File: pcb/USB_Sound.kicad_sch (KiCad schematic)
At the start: 36 parts, among them IC1 PCM2706, J1 USB4500-03-0-A_REVA, J2 Conn_Coaxial_x2, U5 FSUSB42MUX, U6 24AA02-OT, Y1 Crystal

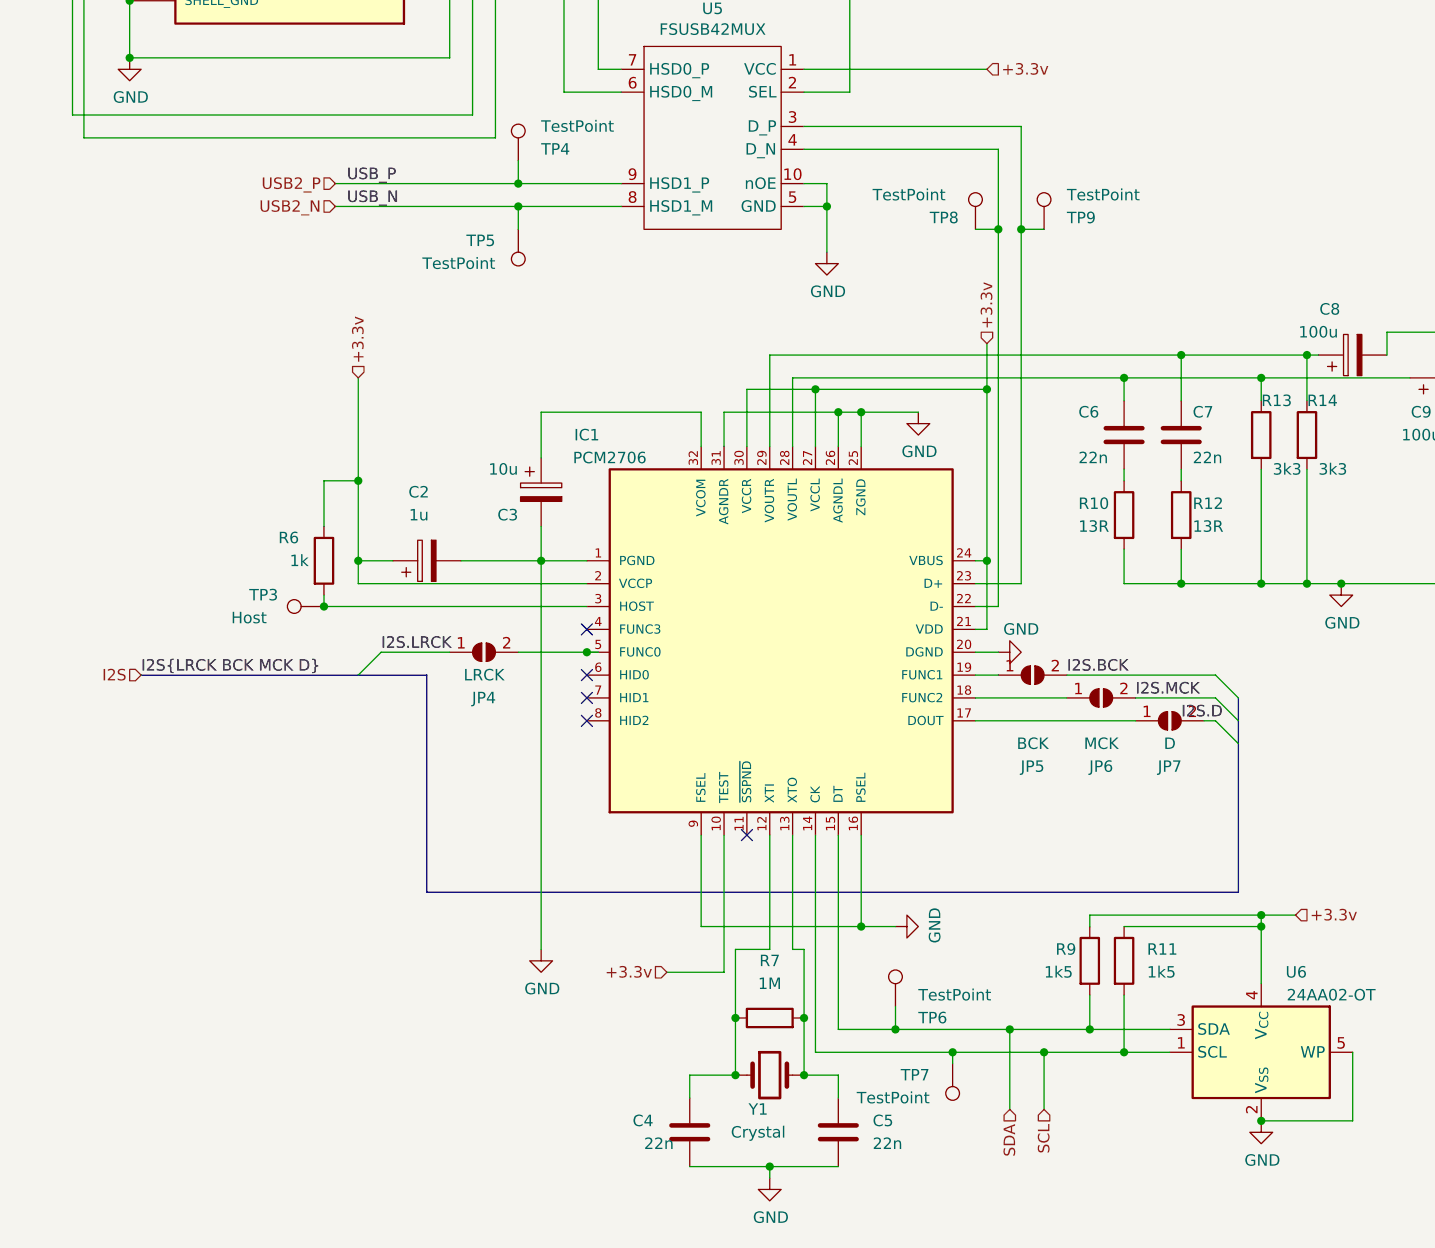
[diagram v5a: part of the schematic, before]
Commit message: - cleanup ERC errors
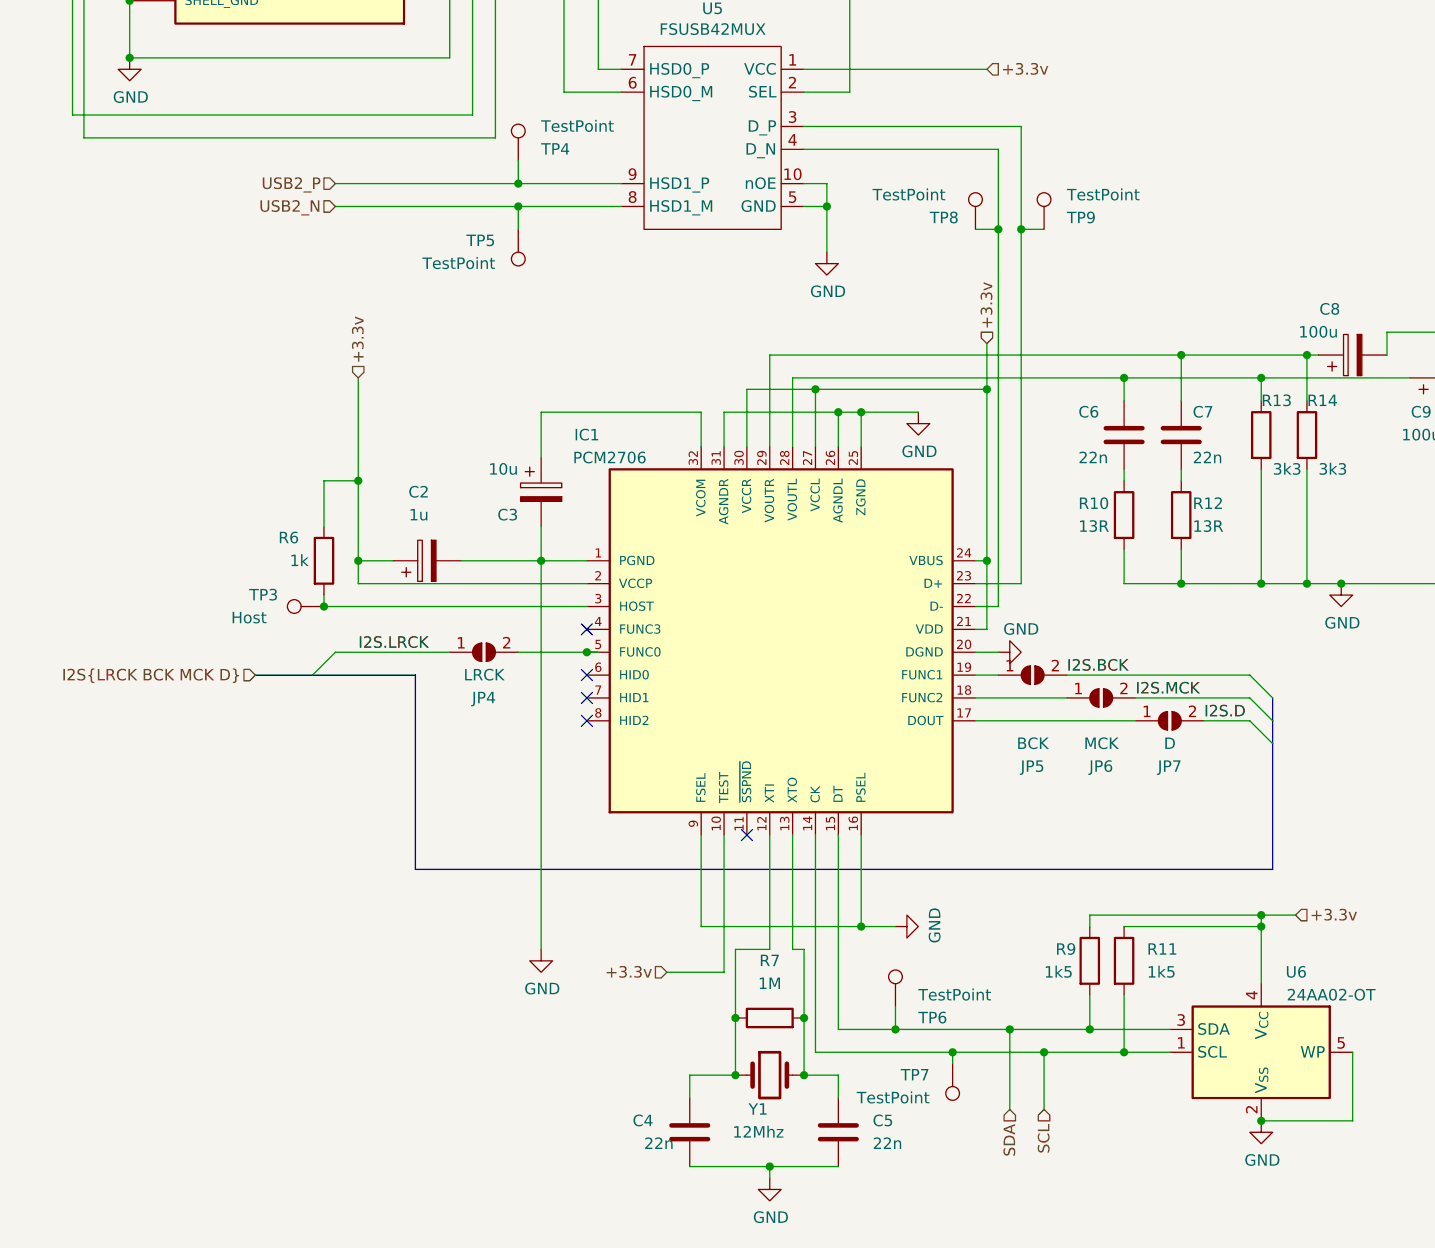
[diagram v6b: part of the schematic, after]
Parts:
- C2, C3, C8, C9: footprint (none) -> Capacitor_SMD:CP_Elec_6.3x7.7
- IC1: footprint Libraries:TQFP32-08 -> Footprints:TQFP32-08
- J1: footprint USB4500-03-0-A_REVA:GCT_USB4500-03-0-A_REVA -> Footprints:GCT_USB4500-03-0-A_REVA
- Y1: value Crystal -> 12Mhz; footprint (none) -> Crystal:Crystal_SMD_Abracon_ABM3-2Pin_5.0x3.2mm_HandSoldering; Farnell (none) -> 2101327
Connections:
- net I2S.D: now also JP7.2 (B)
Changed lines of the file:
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@@
   (no_connect (at 60.96 48.26))
   (no_connect (at 76.2 135.89))
-  (bus_entry (at 148.59 140.97) (size -2.54 -2.54)
-    (stroke (width 0) (type default))
-  )
-  (bus_entry (at 148.59 143.51) (size -2.54 -2.54)
-    (stroke (width 0) (type default))
-  )
-  (bus_entry (at 50.8 135.89) (size 2.54 -2.54)
-    (stroke (width 0) (type default))
-  )
-  (bus_entry (at 148.59 138.43) (size -2.54 -2.54)
+  (bus_entry (at 152.4 143.51) (size -2.54 -2.54)
+    (stroke (width 0) (type default))
+  )
+  (bus_entry (at 45.72 135.89) (size 2.54 -2.54)
+    (stroke (width 0) (type default))
+  )
+  (bus_entry (at 152.4 140.97) (size -2.54 -2.54)
+    (stroke (width 0) (type default))
+  )
+  (bus_entry (at 152.4 138.43) (size -2.54 -2.54)
     (stroke (width 0) (type default))
   )
@@
     (stroke (width 0) (type default))
   )
+  (bus (pts (xy 39.37 135.89) (xy 45.72 135.89))
+    (stroke (width 0) (type default))
+  )
   (wire (pts (xy 96.52 190.5) (xy 96.52 191.77))
     (stroke (width 0) (type default))
@@
     (stroke (width 0) (type default))
   )
-  (wire (pts (xy 53.34 133.35) (xy 60.96 133.35))
-    (stroke (width 0) (type default))
-  )
   (wire (pts (xy 68.58 83.82) (xy 80.01 83.82))
     (stroke (width 0) (type default))
@@
     (stroke (width 0) (type default))
   )
+  (bus (pts (xy 45.72 135.89) (xy 57.15 135.89))
+    (stroke (width 0) (type default))
+  )
   (wire (pts (xy 91.44 106.68) (xy 91.44 110.49))
     (stroke (width 0) (type default))
@@
     (stroke (width 0) (type default))
   )
-  (bus (pts (xy 58.42 160.02) (xy 58.42 135.89))
-    (stroke (width 0) (type default))
-  )
   (wire (pts (xy 119.38 135.89) (xy 121.92 135.89))
     (stroke (width 0) (type default))
@@
     (stroke (width 0) (type default))
   )
+  (wire (pts (xy 137.16 138.43) (xy 149.86 138.43))
+    (stroke (width 0) (type default))
+  )
   (wire (pts (xy 87.63 180.34) (xy 87.63 182.88))
     (stroke (width 0) (type default))
@@
     (stroke (width 0) (type default))
   )
+  (wire (pts (xy 149.86 135.89) (xy 129.54 135.89))
+    (stroke (width 0) (type default))
+  )
   (wire (pts (xy 100.33 83.82) (xy 102.87 83.82))
     (stroke (width 0) (type default))
   )
-  (wire (pts (xy 137.16 138.43) (xy 146.05 138.43))
-    (stroke (width 0) (type default))
-  )
   (wire (pts (xy 25.4 55.88) (xy 25.4 60.96))
     (stroke (width 0) (type default))
@@
     (stroke (width 0) (type default))
   )
-  (bus (pts (xy 50.8 135.89) (xy 58.42 135.89))
-    (stroke (width 0) (type default))
-  )
   (wire (pts (xy 101.6 104.14) (xy 93.98 104.14))
     (stroke (width 0) (type default))
@@
     (stroke (width 0) (type default))
   )
+  (wire (pts (xy 144.78 140.97) (xy 149.86 140.97))
+    (stroke (width 0) (type default))
+  )
   (wire (pts (xy 120.65 104.14) (xy 120.65 123.19))
     (stroke (width 0) (type default))
@@
     (stroke (width 0) (type default))
   )
-  (bus (pts (xy 148.59 160.02) (xy 58.42 160.02))
-    (stroke (width 0) (type default))
-  )
   (wire (pts (xy 62.23 123.19) (xy 71.12 123.19))
     (stroke (width 0) (type default))
   )
-  (wire (pts (xy 146.05 135.89) (xy 129.54 135.89))
-    (stroke (width 0) (type default))
-  )
   (wire (pts (xy 104.14 190.5) (xy 96.52 190.5))
     (stroke (width 0) (type default))
@@
     (stroke (width 0) (type default))
   )
+  (bus (pts (xy 57.15 135.89) (xy 57.15 157.48))
+    (stroke (width 0) (type default))
+  )
   (wire (pts (xy 132.08 171.45) (xy 132.08 175.26))
     (stroke (width 0) (type default))
@@
     (stroke (width 0) (type default))
   )
-  (bus (pts (xy 148.59 143.51) (xy 148.59 160.02))
-    (stroke (width 0) (type default))
-  )
   (wire (pts (xy 101.6 153.67) (xy 101.6 177.8))
     (stroke (width 0) (type default))
@@
     (stroke (width 0) (type default))
   )
-  (bus (pts (xy 26.67 135.89) (xy 50.8 135.89))
-    (stroke (width 0) (type default))
-  )
   (wire (pts (xy 25.4 67.31) (xy 25.4 60.96))
     (stroke (width 0) (type default))
@@
     (stroke (width 0) (type default))
   )
+  (wire (pts (xy 48.26 133.35) (xy 60.96 133.35))
+    (stroke (width 0) (type default))
+  )
   (wire (pts (xy 48.26 81.28) (xy 68.58 81.28))
     (stroke (width 0) (type default))
@@
     (stroke (width 0) (type default))
   )
-  (bus (pts (xy 148.59 138.43) (xy 148.59 140.97))
-    (stroke (width 0) (type default))
-  )
   (wire (pts (xy 76.2 133.35) (xy 77.47 133.35))
     (stroke (width 0) (type default))
@@
     (stroke (width 0) (type default))
   )
+  (bus (pts (xy 152.4 143.51) (xy 152.4 157.48))
+    (stroke (width 0) (type default))
+  )
   (wire (pts (xy 50.8 114.3) (xy 50.8 123.19))
     (stroke (width 0) (type default))
@@
     (stroke (width 0) (type default))
   )
+  (bus (pts (xy 152.4 138.43) (xy 152.4 140.97))
+    (stroke (width 0) (type default))
+  )
   (wire (pts (xy 88.9 153.67) (xy 88.9 163.83))
     (stroke (width 0) (type default))
@@
     (stroke (width 0) (type default))
   )
+  (bus (pts (xy 57.15 157.48) (xy 152.4 157.48))
+    (stroke (width 0) (type default))
+  )
   (wire (pts (xy 76.2 128.27) (xy 46.99 128.27))
     (stroke (width 0) (type default))
@@
     (stroke (width 0) (type default))
   )
-  (bus (pts (xy 148.59 140.97) (xy 148.59 143.51))
-    (stroke (width 0) (type default))
-  )
   (wire (pts (xy 92.71 180.34) (xy 87.63 180.34))
     (stroke (width 0) (type default))
@@
     (stroke (width 0) (type default))
   )
+  (bus (pts (xy 152.4 140.97) (xy 152.4 143.51))
+    (stroke (width 0) (type default))
+  )
   (wire (pts (xy 106.68 163.83) (xy 110.49 163.83))
     (stroke (width 0) (type default))
@@
     (stroke (width 0) (type default))
   )
-  (wire (pts (xy 144.78 140.97) (xy 146.05 140.97))
-    (stroke (width 0) (type default))
-  )
   (wire (pts (xy 135.89 102.87) (xy 151.13 102.87))
     (stroke (width 0) (type default))
@@
   (wire (pts (xy 119.38 130.81) (xy 120.65 130.81))
     (stroke (width 0) (type default))
-  )
-  (label "I2S{LRCK BCK MCK D}" (at 26.67 135.89 0) (fields_autoplaced)
-    (effects (font (size 1.27 1.27)) (justify left bottom))
   )
   (label "I2S.MCK" (at 137.16 138.43 0)
     (effects (font (size 1.27 1.27)) (justify left bottom))
   )
-  (label "USB_P" (at 49.53 81.28 0) (fields_autoplaced)
-    (effects (font (size 1.27 1.27)) (justify left bottom))
-  )
   (label "USBD_P" (at 69.85 43.18 0) (fields_autoplaced)
     (effects (font (size 1.27 1.27)) (justify left bottom))
   )
-  (label "I2S.D" (at 142.24 140.97 0)
-    (effects (font (size 1.27 1.27)) (justify left bottom))
-  )
   (label "USBD_N" (at 69.85 45.72 0) (fields_autoplaced)
     (effects (font (size 1.27 1.27)) (justify left bottom))
   )
-  (label "I2S.LRCK" (at 53.34 133.35 0)
+  (label "I2S.LRCK" (at 50.8 133.35 0)
     (effects (font (size 1.27 1.27)) (justify left bottom))
   )
-  (label "USB_N" (at 49.53 83.82 0) (fields_autoplaced)
+  (label "I2S.D" (at 144.78 140.97 0)
     (effects (font (size 1.27 1.27)) (justify left bottom))
   )
@@
     (effects (font (size 1.27 1.27)) (justify left))
   )
-  (hierarchical_label "I2S" (shape input) (at 26.67 135.89 180) (fields_autoplaced)
+  (hierarchical_label "I2S{LRCK BCK MCK D}" (shape input) (at 39.37 135.89 180) (fields_autoplaced)
     (effects (font (size 1.27 1.27)) (justify right))
   )
@@
       (effects (font (size 1.27 1.27)) (justify right))
     )
-    (property "Footprint" "" (at 72.0852 119.38 0)
+    (property "Footprint" "Capacitor_SMD:CP_Elec_6.3x7.7" (at 72.0852 119.38 0)
       (effects (font (size 1.27 1.27)) hide)
     )
@@
       (effects (font (size 1.27 1.27)))
     )
-    (property "Footprint" "" (at 175.26 101.9048 0)
+    (property "Footprint" "Capacitor_SMD:CP_Elec_6.3x7.7" (at 175.26 101.9048 0)
       (effects (font (size 1.27 1.27)) hide)
     )
@@
       (effects (font (size 1.27 1.27)))
     )
-    (property "Footprint" "" (at 62.23 122.2248 0)
+    (property "Footprint" "Capacitor_SMD:CP_Elec_6.3x7.7" (at 62.23 122.2248 0)
       (effects (font (size 1.27 1.27)) hide)
     )
@@
       (effects (font (size 1.27 1.27)))
     )
-    (property "Footprint" "Libraries:TQFP32-08" (at 99.06 130.81 0)
+    (property "Footprint" "Footprints:TQFP32-08" (at 99.06 130.81 0)
       (effects (font (size 1.27 1.27)) (justify bottom) hide)
     )
@@
       (effects (font (size 1.27 1.27)))
     )
-    (property "Footprint" "USB4500-03-0-A_REVA:GCT_USB4500-03-0-A_REVA" (at 43.18 45.72 0)
+    (property "Footprint" "Footprints:GCT_USB4500-03-0-A_REVA" (at 43.18 45.72 0)
       (effects (font (size 1.27 1.27)) (justify bottom) hide)
     )
@@
       (effects (font (size 1.27 1.27)))
     )
-    (property "Value" "Crystal" (at 95.25 186.69 0)
-      (effects (font (size 1.27 1.27)))
-    )
-    (property "Footprint" "" (at 96.52 180.34 0)
+    (property "Value" "12Mhz" (at 95.25 186.69 0)
+      (effects (font (size 1.27 1.27)))
+    )
+    (property "Footprint" "Crystal:Crystal_SMD_Abracon_ABM3-2Pin_5.0x3.2mm_HandSoldering" (at 96.52 180.34 0)
       (effects (font (size 1.27 1.27)) hide)
     )
     (property "Datasheet" "~" (at 96.52 180.34 0)
+      (effects (font (size 1.27 1.27)) hide)
+    )
+    (property "Farnell" "2101327" (at 96.52 180.34 0)
       (effects (font (size 1.27 1.27)) hide)
     )
@@
       (effects (font (size 1.27 1.27)))
     )
-    (property "Footprint" "" (at 165.1 99.3648 0)
-      (effects (font (size 1.27 1.27)) hide)
-    )
+    (property "Footprint" "Capacitor_SMD:CP_Elec_6.3x7.7" (at 165.1 99.3648 0)
+      (effects (font (size 1.27 1.27)) hide)
+    )
